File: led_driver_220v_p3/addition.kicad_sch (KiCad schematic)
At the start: 3 parts, among them J13 D, J14 V

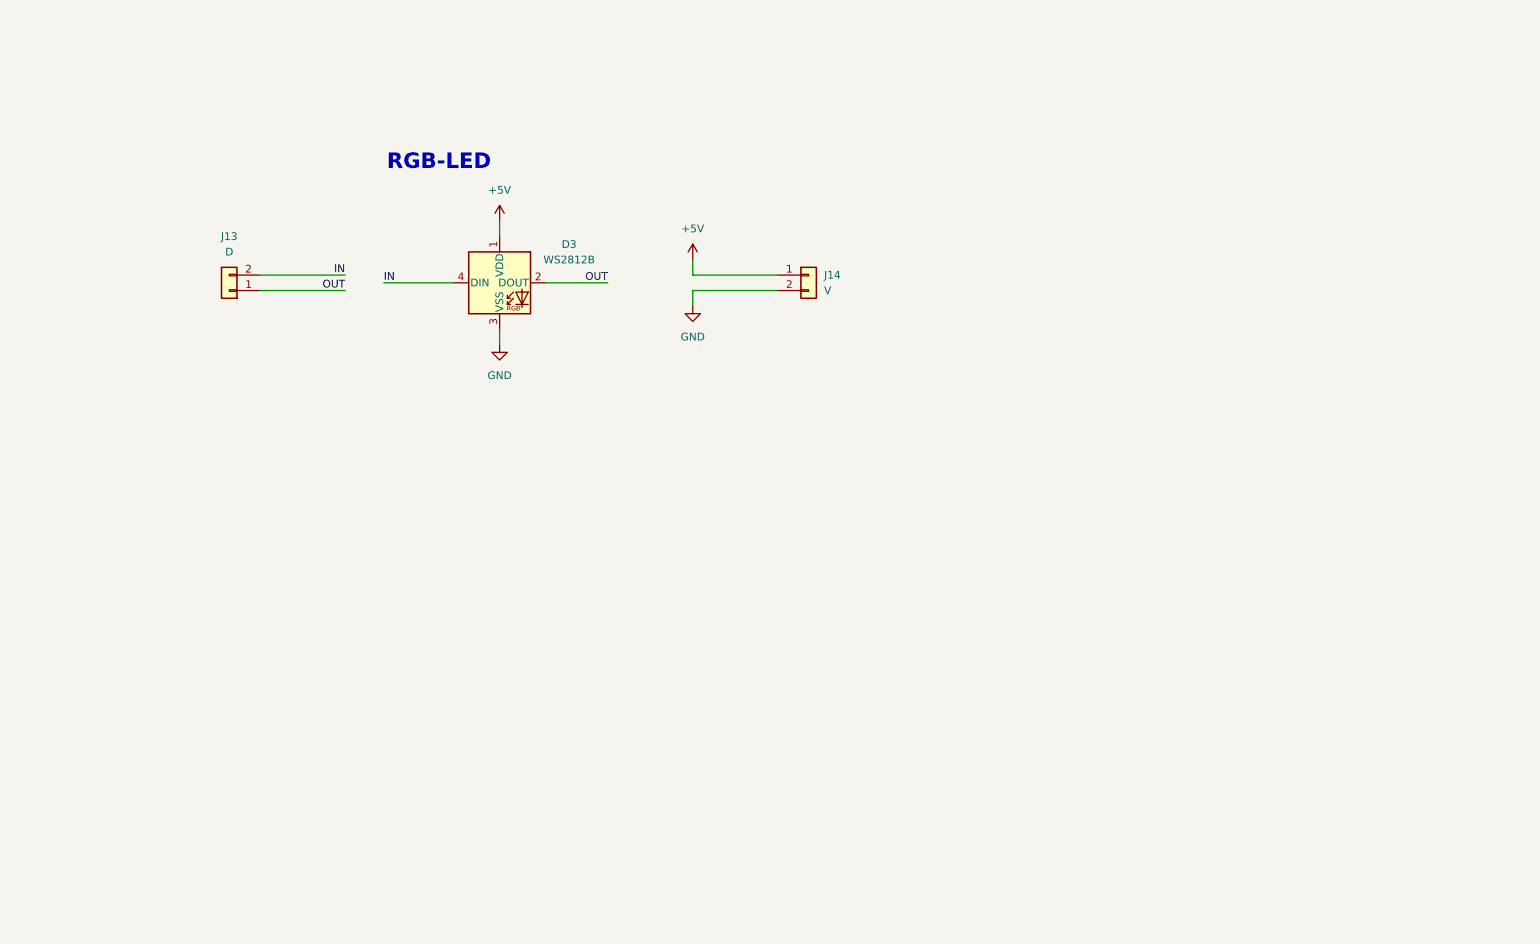
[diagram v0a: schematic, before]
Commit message: led_driver_220v_p3 update
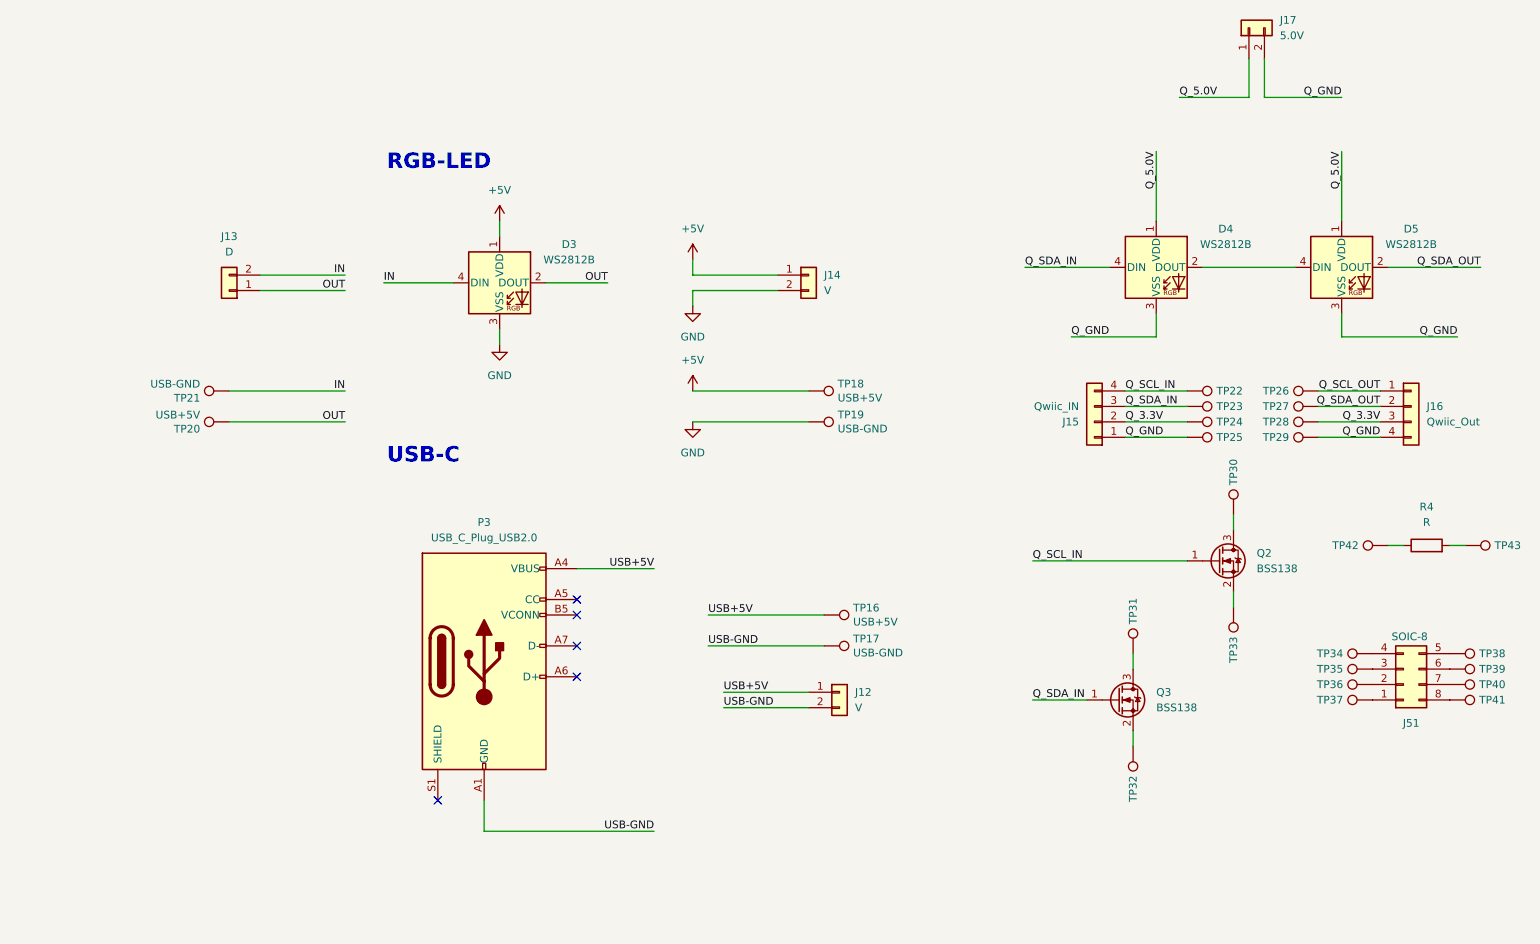
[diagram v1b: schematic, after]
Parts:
- added D4, D5: WS2812B, LED_SMD:LED_WS2812B_PLCC4_5.0x5.0mm_P3.2mm, symbol LED:WS2812B
- added J12: V, Connector_PinHeader_2.54mm:PinHeader_1x02_P2.54mm_Vertical, symbol Connector_Generic:Conn_01x02
- added J15: Qwiic_IN, Connector_JST:JST_SH_SM04B-SRSS-TB_1x04-1MP_P1.00mm_Horizontal, symbol Connector_Generic:Conn_01x04
- added J16: Qwiic_Out, Connector_JST:JST_SH_SM04B-SRSS-TB_1x04-1MP_P1.00mm_Horizontal, symbol Connector_Generic:Conn_01x04
- added J17: 5.0V, Connector_PinHeader_1.27mm:PinHeader_1x02_P1.27mm_Vertical, symbol Connector_Generic:Conn_01x02
- added J51: SOIC-8, Package_SO:SO-8_3.9x4.9mm_P1.27mm, symbol Connector_Generic:Conn_02x04_Counter_Clockwise
- added P3: USB_C_Plug_USB2.0, zhaw:USB_C_DEALON_009, symbol Connector:USB_C_Plug_USB2.0
- added Q2, Q3: BSS138, Package_TO_SOT_SMD:SOT-23, symbol Transistor_FET:BSS138
- added R4: R, Resistor_SMD:R_1206_3216Metric_Pad1.30x1.75mm_HandSolder, symbol Device:R
- added TP16, TP18, TP20: USB+5V, TestPoint:TestPoint_Pad_1.5x1.5mm, symbol Connector:TestPoint
- added TP17, TP19, TP21: USB-GND, TestPoint:TestPoint_Pad_1.5x1.5mm, symbol Connector:TestPoint
- added TP22, TP23, TP24, TP25, TP26, TP27, TP28, TP29: ~, TestPoint:TestPoint_THTPad_D1.5mm_Drill0.7mm, symbol Connector:TestPoint
- added TP30, TP31, TP32, TP33, TP34, TP35, TP36, TP37, TP38, TP39, TP40, TP41, TP42, TP43: ~, TestPoint:TestPoint_Pad_D1.0mm, symbol Connector:TestPoint
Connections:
- net +5V: now also TP18.1
- net GND: now also TP19.1
- net IN: now also TP21.1
- net OUT: now also TP20.1
- new net: Q2.3 (D), TP30.1
- new net: R4.1, TP42.1
- new net: R4.2, TP43.1
- new net: J51.7 (Pin_7), TP40.1
- new net: J51.1 (Pin_1), TP37.1
- new net: J51.2 (Pin_2), TP36.1
- new net: J51.3 (Pin_3), TP35.1
- new net: J51.4 (Pin_4), TP34.1
- new net: J51.5 (Pin_5), TP38.1
- new net: J51.6 (Pin_6), TP39.1
- new net: J51.8 (Pin_8), TP41.1
- new net: D4.2 (DOUT), D5.4 (DIN)
- new net: Q2.2 (S), TP33.1
- new net: Q3.3 (D), TP31.1
- new net: Q3.2 (S), TP32.1
- new net Q_3.3V: J15.2 (Pin_2), J16.3 (Pin_3), TP24.1, TP28.1
- new net Q_5.0V: D4.1 (VDD), D5.1 (VDD), J17.1 (Pin_1)
- new net Q_GND: D4.3 (VSS), D5.3 (VSS), J15.1 (Pin_1), J16.4 (Pin_4), J17.2 (Pin_2), TP25.1, TP29.1
- new net Q_SCL_IN: J15.4 (Pin_4), Q2.1 (G), TP22.1
- new net Q_SCL_OUT: J16.1 (Pin_1), TP26.1
- new net Q_SDA_IN: D4.4 (DIN), J15.3 (Pin_3), Q3.1 (G), TP23.1
- new net Q_SDA_OUT: D5.2 (DOUT), J16.2 (Pin_2), TP27.1
- new net USB+5V: J12.1 (Pin_1), P3.A4 (VBUS), P3.A9 (VBUS), P3.B4 (VBUS), P3.B9 (VBUS), TP16.1
- new net USB-GND: J12.2 (Pin_2), P3.A1 (GND), P3.A12 (GND), P3.B1 (GND), P3.B12 (GND), TP17.1
- no-connect marks 0 -> 5
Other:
- note added: "USB-C"

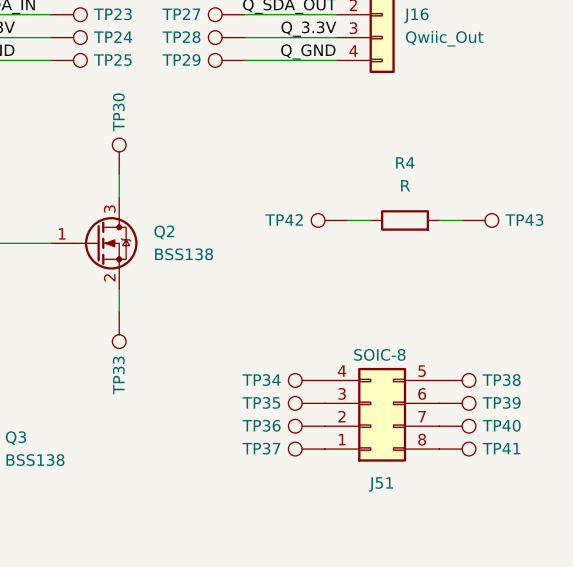
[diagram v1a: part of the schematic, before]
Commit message: led_driver_220v_p3 update
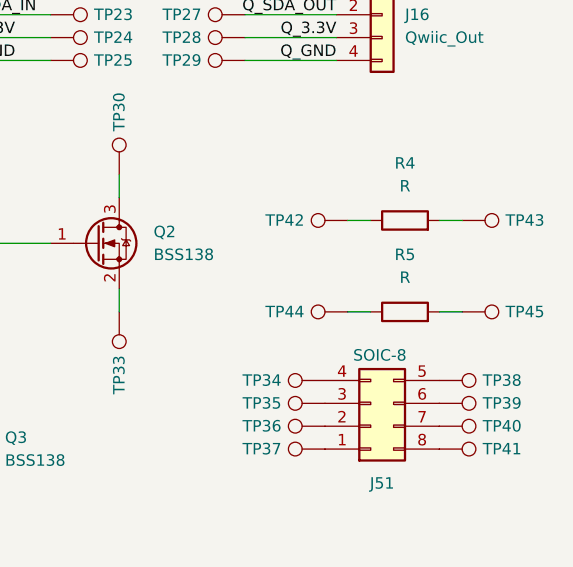
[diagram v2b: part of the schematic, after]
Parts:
- added R5: R, Resistor_SMD:R_0805_2012Metric_Pad1.20x1.40mm_HandSolder, symbol Device:R
- added TP44, TP45: ~, TestPoint:TestPoint_Pad_D1.0mm, symbol Connector:TestPoint
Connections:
- new net: R5.1, TP44.1
- new net: R5.2, TP45.1
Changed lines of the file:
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@@
 	(wire
 		(pts
+			(xy 255.27 128.27) (xy 257.81 128.27)
+		)
+		(stroke
+			(width 0)
+			(type default)
+		)
+	)
+	(wire
+		(pts
 			(xy 143.51 129.54) (xy 162.56 129.54)
 		)
@@
 	(wire
 		(pts
+			(xy 265.43 128.27) (xy 267.97 128.27)
+		)
+		(stroke
+			(width 0)
+			(type default)
+		)
+	)
+	(wire
+		(pts
 			(xy 212.09 97.79) (xy 222.25 97.79)
 		)
@@
 	(symbol
 		(lib_id "Connector:TestPoint")
+		(at 255.27 128.27 90)
+		(mirror x)
+		(unit 1)
+		(exclude_from_sim no)
+		(in_bom yes)
+		(on_board yes)
+		(dnp no)
+		(property "Reference" "TP44"
+			(at 250.444 128.27 90)
+			(effects
+				(font
+					(size 1.27 1.27)
+				)
+				(justify left)
+			)
+		)
+		(property "Value" "~"
+			(at 250.4948 129.413 90)
+			(effects
+				(font
+					(size 1.27 1.27)
+				)
+				(justify left)
+			)
+		)
+		(property "Footprint" "TestPoint:TestPoint_Pad_D1.0mm"
+			(at 255.27 133.35 0)
+			(effects
+				(font
+					(size 1.27 1.27)
+				)
+				(hide yes)
+			)
+		)
+		(property "Datasheet" "~"
+			(at 255.27 133.35 0)
+			(effects
+				(font
+					(size 1.27 1.27)
+				)
+				(hide yes)
+			)
+		)
+		(property "Description" ""
+			(at 255.27 128.27 0)
+			(effects
+				(font
+					(size 1.27 1.27)
+				)
+			)
+		)
+		(pin "1"
+		)
+		(instances
+			(project "led_driver_220v_p3"
+				(path "/73fbfc2f-6207-4cf0-8939-c74998e2b107/d428b32d-6d2b-484f-a727-4bbeb5521592"
+					(reference "TP44")
+					(unit 1)
+				)
+			)
+		)
+	)
+	(symbol
+		(lib_id "Connector:TestPoint")
 		(at 265.43 140.97 270)
 		(unit 1)
@@
 	)
 	(symbol
+		(lib_id "Device:R")
+		(at 261.62 128.27 90)
+		(unit 1)
+		(exclude_from_sim no)
+		(in_bom yes)
+		(on_board yes)
+		(dnp no)
+		(fields_autoplaced yes)
+		(property "Reference" "R5"
+			(at 261.62 121.92 90)
+			(effects
+				(font
+					(size 1.27 1.27)
+				)
+			)
+		)
+		(property "Value" "R"
+			(at 261.62 124.46 90)
+			(effects
+				(font
+					(size 1.27 1.27)
+				)
+			)
+		)
+		(property "Footprint" "Resistor_SMD:R_0805_2012Metric_Pad1.20x1.40mm_HandSolder"
+			(at 261.62 130.048 90)
+			(effects
+				(font
+					(size 1.27 1.27)
+				)
+				(hide yes)
+			)
+		)
+		(property "Datasheet" "~"
+			(at 261.62 128.27 0)
+			(effects
+				(font
+					(size 1.27 1.27)
+				)
+				(hide yes)
+			)
+		)
+		(property "Description" "Resistor"
+			(at 261.62 128.27 0)
+			(effects
+				(font
+					(size 1.27 1.27)
+				)
+				(hide yes)
+			)
+		)
+		(pin "1"
+		)
+		(pin "2"
+		)
+		(instances
+			(project "led_driver_220v_p3"
+				(path "/73fbfc2f-6207-4cf0-8939-c74998e2b107/d428b32d-6d2b-484f-a727-4bbeb5521592"
+					(reference "R5")
+					(unit 1)
+				)
+			)
+		)
+	)
+	(symbol
 		(lib_id "Connector:TestPoint")
 		(at 160.02 97.79 270)
@@
 					(unit 1)
 				)
+			)
+		)
+	)
+	(symbol
+		(lib_id "Connector:TestPoint")
+		(at 267.97 128.27 270)
+		(unit 1)
+		(exclude_from_sim no)
+		(in_bom yes)
+		(on_board yes)
+		(dnp no)
+		(property "Reference" "TP45"
+			(at 272.796 128.27 90)
+			(effects
+				(font
+					(size 1.27 1.27)
+				)
+				(justify left)
+			)
+		)
+		(property "Value" "~"
+			(at 272.7452 129.413 90)
+			(effects
+				(font
+					(size 1.27 1.27)
+				)
+				(justify left)
+			)
+		)
+		(property "Footprint" "TestPoint:TestPoint_Pad_D1.0mm"
+			(at 267.97 133.35 0)
+			(effects
+				(font
+					(size 1.27 1.27)
+				)
+				(hide yes)
+			)
+		)
+		(property "Datasheet" "~"
+			(at 267.97 133.35 0)
+			(effects
+				(font
+					(size 1.27 1.27)
+				)
+				(hide yes)
+			)
+		)
+		(property "Description" ""
+			(at 267.97 128.27 0)
+			(effects
+				(font
+					(size 1.27 1.27)
+				)
+			)
+		)
+		(pin "1"
+		)
+		(instances
+			(project "led_driver_220v_p3"
+				(path "/73fbfc2f-6207-4cf0-8939-c74998e2b107/d428b32d-6d2b-484f-a727-4bbeb5521592"
+					(reference "TP45")
+					(unit 1)
+				)

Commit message: led_driver_220v_p3 update + gerber
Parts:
- added R6: 56k, Resistor_SMD:R_0805_2012Metric_Pad1.20x1.40mm_HandSolder, symbol Device:R
- added R7: 22k, Resistor_SMD:R_0805_2012Metric_Pad1.20x1.40mm_HandSolder, symbol Device:R
- added R8: R, Resistor_SMD:R_1206_3216Metric_Pad1.30x1.75mm_HandSolder, symbol Device:R
- added R9: R, Resistor_SMD:R_0805_2012Metric_Pad1.20x1.40mm_HandSolder, symbol Device:R
- added TP46, TP47, TP48, TP49: ~, TestPoint:TestPoint_Pad_D1.0mm, symbol Connector:TestPoint
- added U3: SPX3819M5-L, Package_TO_SOT_SMD:SOT-23-5, symbol Regulator_Linear:SPX3819M5-L
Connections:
- net +5V: now also U3.1 (IN), U3.3 (EN)
- net GND: now also R7.2, U3.2 (GND)
- net OUT: now also R6.1, U3.5 (OUT)
- new net: R8.1, TP46.1
- new net: R9.2, TP49.1
- new net: R8.2, TP48.1
- new net: R6.2, R7.1, U3.4 (ADJ)
- new net: R9.1, TP47.1
